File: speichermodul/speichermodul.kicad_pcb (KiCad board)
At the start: 2 copper layers, 100 x 160 mm, 48 parts, among them IC1 6116, P7 CONN_01X01, U1 7400, U2 74LS08, U3 74LS08, U4 74LS14, U5 74LS540, U6 74LS540

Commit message: Kabel verlegen und pcb layout
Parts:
- added P3: CONN_01X01, Pin_Headers:Pin_Header_Straight_1x01_Pitch1.27mm, F.Cu at (24.1, 25.4)
- added P4: CONN_01X01, Pin_Headers:Pin_Header_Straight_1x01_Pitch1.27mm, F.Cu at (30.5, 25.4)
- added SW1: SW_PUSH, Buttons_Switches_ThroughHole:SW_PUSH_6mm_h5mm, F.Cu at (24.1, 134.6)
- added SW2: SW_PUSH, Buttons_Switches_ThroughHole:SW_PUSH_6mm_h5mm, F.Cu at (22.9, 119.4)
- moved R8 23.2 mm to (33.0, 130.8)
- moved R22 7.62 mm to (73.7, 30.5)
- moved D11 5.08 mm to (50.8, 26.7)
- moved R16 5.08 mm to (48.3, 30.5)
- moved R7 4.58 mm to (33.0, 114.3)
- moved D12 3.81 mm to (55.9, 26.7)
- moved D18 3.81 mm to (86.4, 26.7)
- moved R17 3.81 mm to (53.3, 30.5)
- moved R23 3.81 mm to (83.8, 30.5)
- moved R21 3.81 mm to (78.7, 30.5)
- moved D13 2.54 mm to (61.0, 26.7)
- moved R18 2.54 mm to (58.4, 30.5)
- moved D16 2.54 mm to (81.3, 26.7)
- moved D14 1.27 mm to (66.0, 26.7)
- moved R19 1.27 mm to (63.5, 30.5)
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
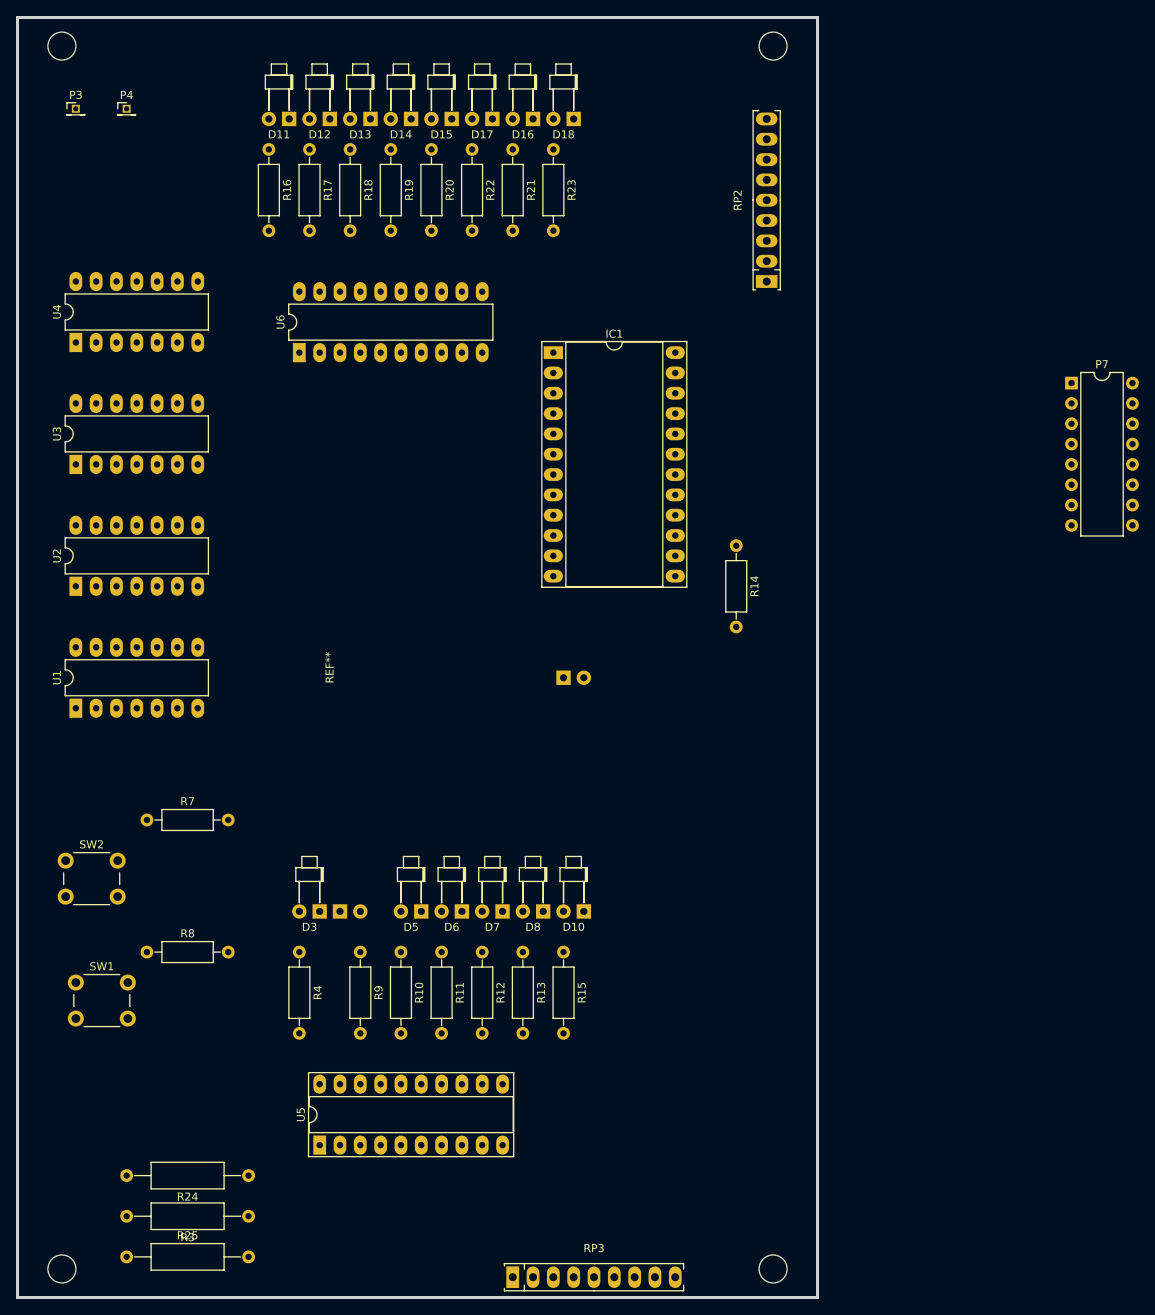
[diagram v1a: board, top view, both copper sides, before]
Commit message: Pcb layout perfektioniert und schaltplan vorangetrieben
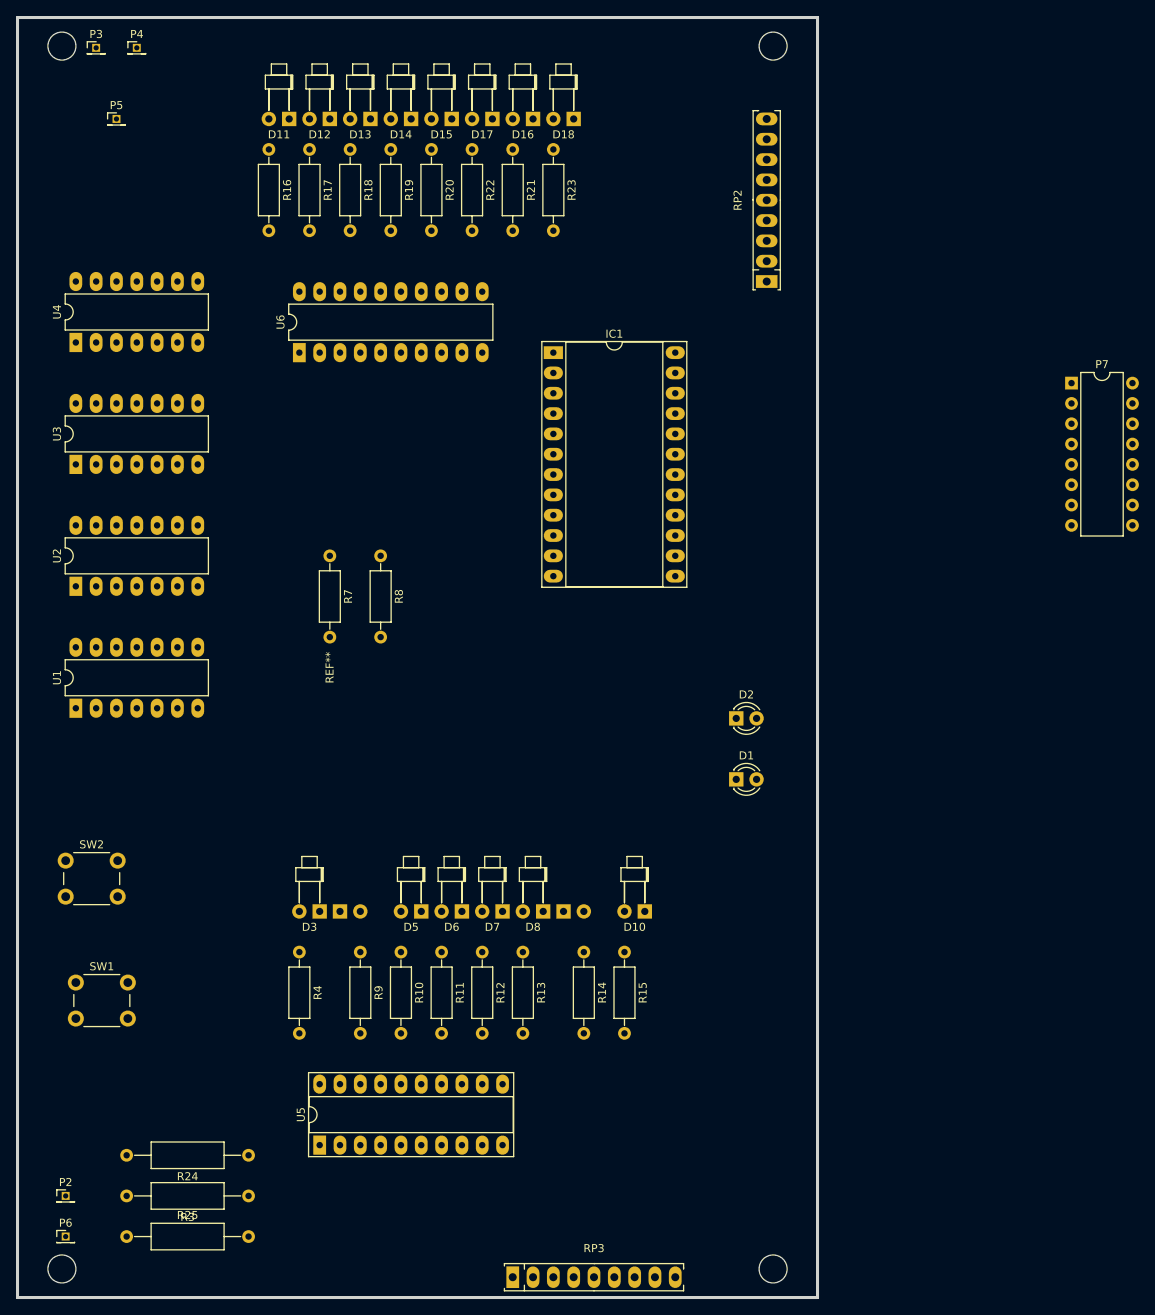
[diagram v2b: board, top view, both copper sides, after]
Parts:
- added D1: LED, LEDs:LED_D3.0mm, F.Cu at (106.7, 109.2)
- added D2: LED, LEDs:LED_D3.0mm, F.Cu at (106.7, 101.6)
- added P2: CONN_01X01, Pin_Headers:Pin_Header_Straight_1x01_Pitch1.27mm, F.Cu at (22.9, 161.3)
- added P5: CONN_01X01, Pin_Headers:Pin_Header_Straight_1x01_Pitch1.27mm, F.Cu at (29.2, 26.7)
- added P6: CONN_01X01, Pin_Headers:Pin_Header_Straight_1x01_Pitch1.27mm, F.Cu at (22.9, 166.4)
- moved R8 57.5 mm to (62.2, 81.3), turned to 270 degrees
- moved R14 54.3 mm to (87.6, 130.8)
- moved R7 40.2 mm to (55.9, 81.3), turned to 270 degrees
- moved D9 29.2 mm to (85.1, 125.7)
- moved P3 8.03 mm to (26.7, 17.8)
- moved P4 7.73 mm to (31.8, 17.8)
- moved D10 7.62 mm to (95.2, 125.7)
- moved R15 7.62 mm to (92.7, 130.8)
- moved R3 2.54 mm to (45.7, 161.3)
- moved R24 2.54 mm to (45.7, 156.2)
- moved R25 2.54 mm to (30.5, 166.4)
